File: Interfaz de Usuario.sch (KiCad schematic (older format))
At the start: 10 parts, among them J2 Conn_01x14, J3 Conn_02x04_Odd_Even, SW1 SW_Push_Dual

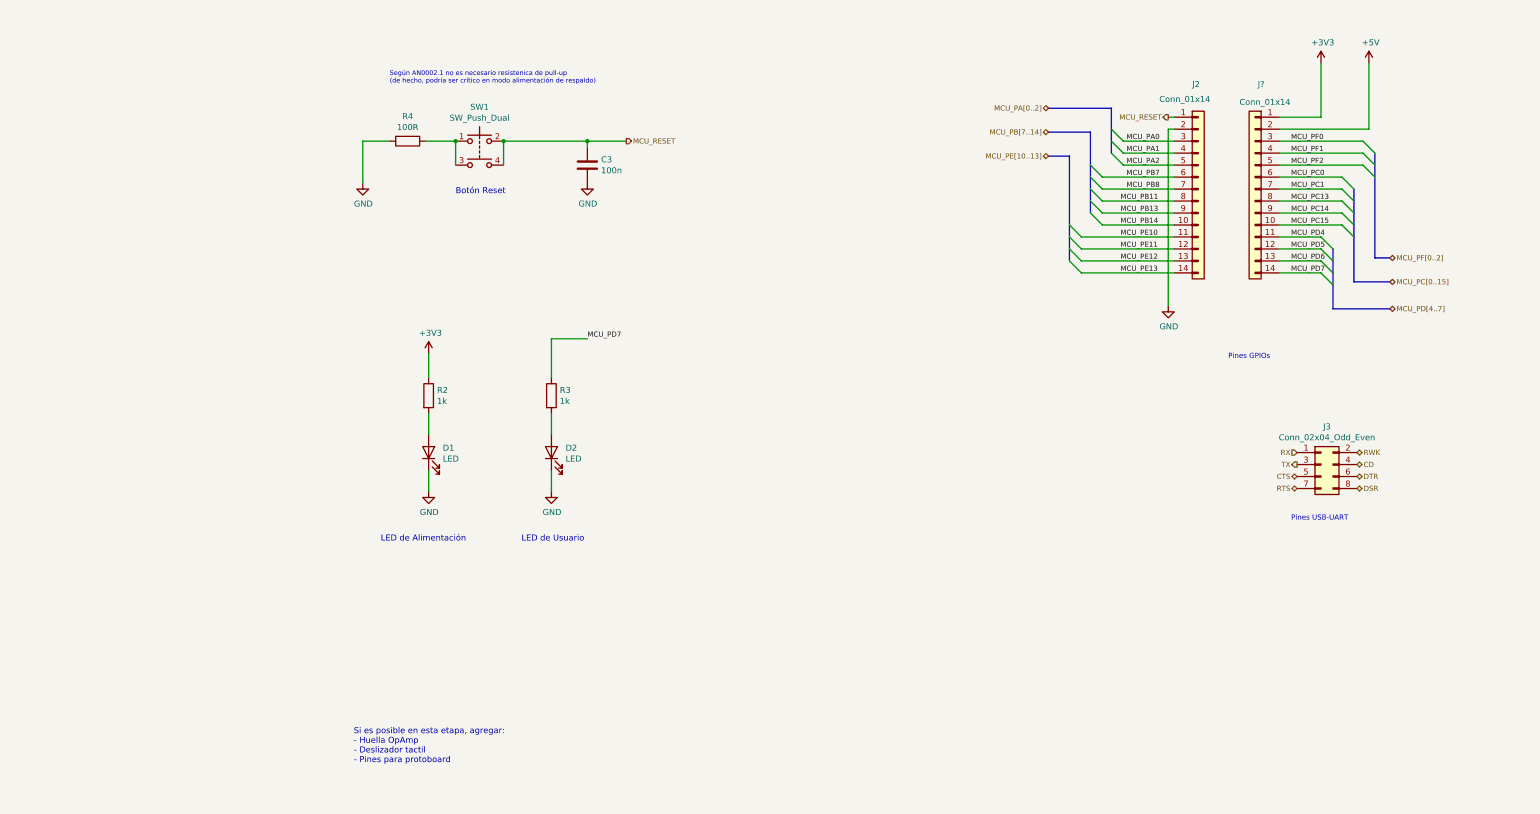
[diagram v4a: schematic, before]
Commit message: Issue #1: Incorporación de conector para debug
Se agrega el conector estandar para ARM de 10 pines para debug con SWD.
Como referencia use la nota de aplicación AN0002.1
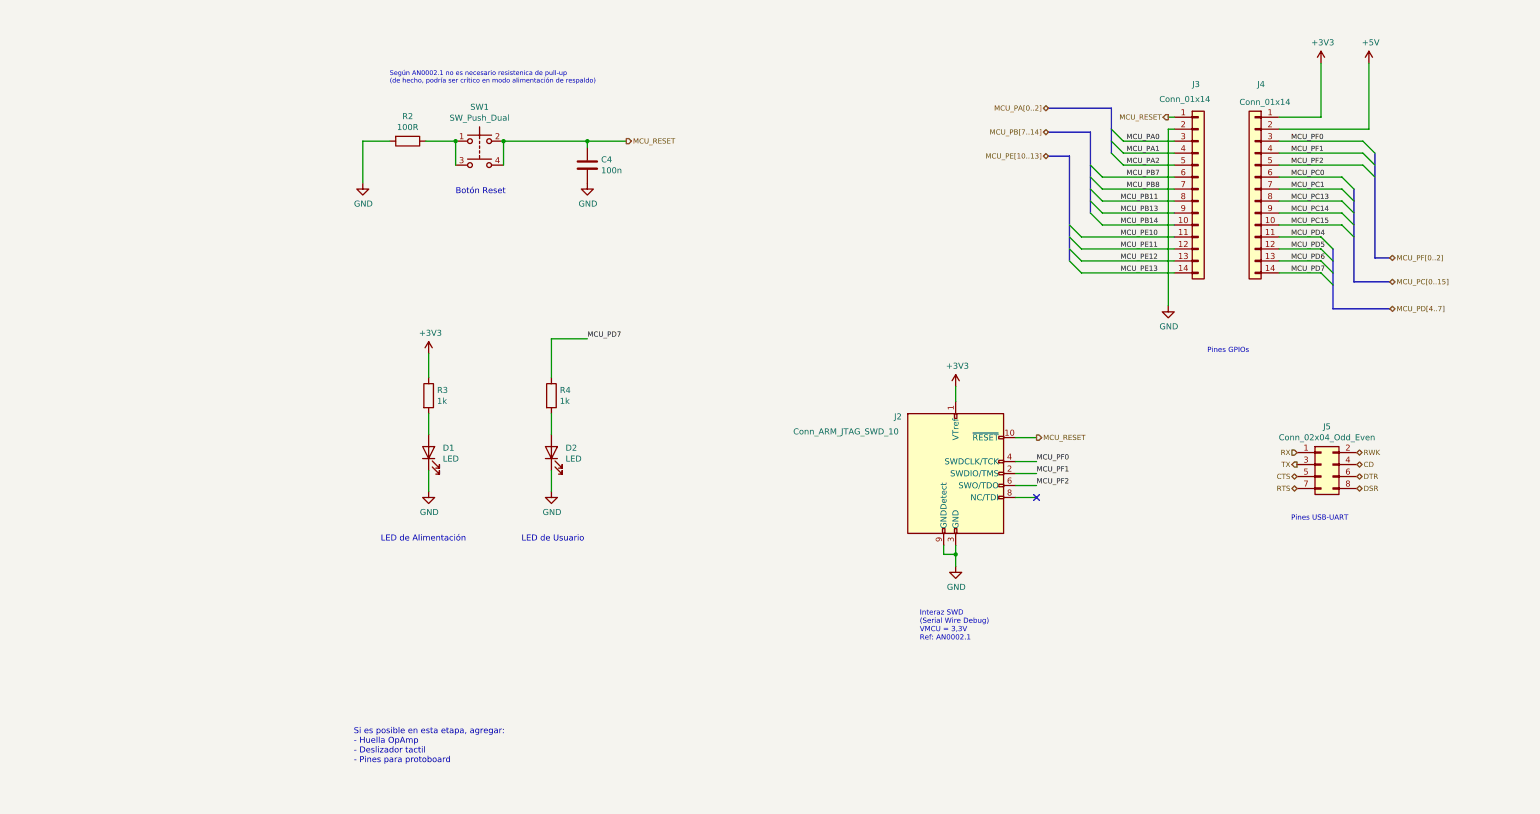
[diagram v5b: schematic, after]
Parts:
- added J2: Conn_ARM_JTAG_SWD_10, symbol Connector:Conn_ARM_JTAG_SWD_10
- gave numbers to parts that had none: 1
- renumbered C3 to C4, J2 to J3, J3 to J5, R4 to R2, R2 to R3, R3 to R4
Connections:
- net +3V3: now also J2.1 (VTref)
- net GND: now also J2.3 (GND), J2.5 (GND), J2.9 (GNDDetect)
- net MCU_PF0: now also J2.4 (SWDCLK/TCK)
- net MCU_PF1: now also J2.2 (SWDIO/TMS)
- net MCU_PF2: now also J2.6 (SWO/TDO)
- net MCU_RESET: now also J2.10 (~RESET~)
- no-connect marks 0 -> 1
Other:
- note added: "Interaz SWD\n(Serial Wire Debug)\nVMCU = 3,3V\nRef: AN0002.1"
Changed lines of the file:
@@
 $EndComp
 $Comp
-L Device:R R2
+L Device:R R3
 U 1 1 5F5B165F
 P 1600 4075
-F 0 "R2" H 1670 4121 50  0000 L CNN
+F 0 "R3" H 1670 4121 50  0000 L CNN
 F 1 "1k" H 1670 4030 50  0000 L CNN
 F 2 "" V 1530 4075 50  0001 C CNN
@@
 LED de Alimentación
 $Comp
-L power:+3V3 #PWR016
+L power:+3V3 #PWR015
 U 1 1 5F5B2737
 P 1600 3725
-F 0 "#PWR016" H 1600 3575 50  0001 C CNN
+F 0 "#PWR015" H 1600 3575 50  0001 C CNN
 F 1 "+3V3" H 1615 3898 50  0000 C CNN
 F 2 "" H 1600 3725 50  0001 C CNN
@@
 Pines USB-UART\n
 $Comp
-L power:+3V3 #PWR021
+L power:+3V3 #PWR022
 U 1 1 5F5DFF8C
 P 9050 1300
-F 0 "#PWR021" H 9050 1150 50  0001 C CNN
+F 0 "#PWR022" H 9050 1150 50  0001 C CNN
 F 1 "+3V3" H 9065 1473 50  0000 C CNN
 F 2 "" H 9050 1300 50  0001 C CNN
@@
 $EndComp
 $Comp
-L power:+5V #PWR022
+L power:+5V #PWR023
 U 1 1 5F5E0DA7
 P 9450 1300
-F 0 "#PWR022" H 9450 1150 50  0001 C CNN
+F 0 "#PWR023" H 9450 1150 50  0001 C CNN
 F 1 "+5V" H 9465 1473 50  0000 C CNN
 F 2 "" H 9450 1300 50  0001 C CNN
@@
 $EndComp
 $Comp
-L power:GND #PWR017
+L power:GND #PWR016
 U 1 1 5F5E177A
 P 1600 4875
-F 0 "#PWR017" H 1600 4625 50  0001 C CNN
+F 0 "#PWR016" H 1600 4625 50  0001 C CNN
 F 1 "GND" H 1605 4702 50  0000 C CNN
 F 2 "" H 1600 4875 50  0001 C CNN
@@
 $EndComp
 $Comp
-L power:GND #PWR020
+L power:GND #PWR021
 U 1 1 5F5E1C7B
 P 7775 3325
-F 0 "#PWR020" H 7775 3075 50  0001 C CNN
+F 0 "#PWR021" H 7775 3075 50  0001 C CNN
 F 1 "GND" H 7780 3152 50  0000 C CNN
 F 2 "" H 7775 3325 50  0001 C CNN
@@
 $EndComp
 $Comp
-L power:GND #PWR018
+L power:GND #PWR017
 U 1 1 5F61283E
 P 2625 4875
-F 0 "#PWR018" H 2625 4625 50  0001 C CNN
+F 0 "#PWR017" H 2625 4625 50  0001 C CNN
 F 1 "GND" H 2630 4702 50  0000 C CNN
 F 2 "" H 2625 4875 50  0001 C CNN
@@
 MCU_PD7
 $Comp
-L Device:R R3
+L Device:R R4
 U 1 1 5F61282A
 P 2625 4075
-F 0 "R3" H 2695 4121 50  0000 L CNN
+F 0 "R4" H 2695 4121 50  0000 L CNN
 F 1 "1k" H 2695 4030 50  0000 L CNN
 F 2 "" V 2555 4075 50  0001 C CNN
@@
 MCU_RESET
 $Comp
-L power:GND #PWR015
+L power:GND #PWR014
 U 1 1 5F61A6A2
 P 1050 2300
-F 0 "#PWR015" H 1050 2050 50  0001 C CNN
+F 0 "#PWR014" H 1050 2050 50  0001 C CNN
 F 1 "GND" H 1055 2127 50  0000 C CNN
 F 2 "" H 1050 2300 50  0001 C CNN
@@
 Wire Wire Line
 	1825 1950 1825 2150
-Text Notes 8275 3775 0    43   ~ 0
+Text Notes 8100 3725 0    43   ~ 0
 Pines GPIOs
 Text Label 7425 1950 0    43   ~ 0
@@
 MCU_RESET
 $Comp
-L Connector_Generic:Conn_02x04_Odd_Even J3
+L Connector_Generic:Conn_02x04_Odd_Even J5
 U 1 1 5F5CD54F
 P 9050 4650
-F 0 "J3" H 9100 4967 50  0000 C CNN
+F 0 "J5" H 9100 4967 50  0000 C CNN
 F 1 "Conn_02x04_Odd_Even" H 9100 4876 50  0000 C CNN
 F 2 "" H 9050 4650 50  0001 C CNN
@@
 Según AN0002.1 no es necesario resistenica de pull-up\n(de hecho, podría ser crítico en modo alimentación de respaldo)
 $Comp
-L Device:C C3
+L Device:C C4
 U 1 1 5F608348
 P 2925 2150
-F 0 "C3" H 3040 2196 50  0000 L CNN
+F 0 "C4" H 3040 2196 50  0000 L CNN
 F 1 "100n" H 3040 2105 50  0000 L CNN
 F 2 "" H 2963 2000 50  0001 C CNN
@@
 $EndComp
 $Comp
-L power:GND #PWR0101
+L power:GND #PWR018
 U 1 1 5F608A3C
 P 2925 2300
-F 0 "#PWR0101" H 2925 2050 50  0001 C CNN
+F 0 "#PWR018" H 2925 2050 50  0001 C CNN
 F 1 "GND" H 2930 2127 50  0000 C CNN
 F 2 "" H 2925 2300 50  0001 C CNN
@@
 $EndComp
 $Comp
-L Device:R R4
+L Device:R R2
 U 1 1 5F60A43B
 P 1425 1950
-F 0 "R4" V 1218 1950 50  0000 C CNN
+F 0 "R2" V 1218 1950 50  0000 C CNN
 F 1 "100R" V 1309 1950 50  0000 C CNN
 F 2 "" V 1355 1950 50  0001 C CNN
@@
 	1050 1950 1050 2300
 $Comp
-L Connector_Generic:Conn_01x14 J2
+L Connector_Generic:Conn_01x14 J3
 U 1 1 5F616B2C
 P 8025 2350
-F 0 "J2" H 7975 3225 50  0000 L CNN
+F 0 "J3" H 7975 3225 50  0000 L CNN
 F 1 "Conn_01x14" H 7700 3100 50  0000 L CNN
 F 2 "" H 8025 2350 50  0001 C CNN
@@
 $EndComp
 $Comp
-L Connector_Generic:Conn_01x14 J?
+L Connector_Generic:Conn_01x14 J4
 U 1 1 5F61A09A
 P 8500 2350
-F 0 "J?" H 8450 3225 50  0000 C CNN
+F 0 "J4" H 8450 3225 50  0000 C CNN
 F 1 "Conn_01x14" H 8418 3076 50  0000 C CNN
 F 2 "" H 8500 2350 50  0001 C CNN
@@
 	-1   0    0    -1
 $EndComp
+$Comp
+L Connector:Conn_ARM_JTAG_SWD_10 J2
+U 1 1 5F61E73C
+P 6000 4725
+F 0 "J2" H 5550 5200 50  0000 R CNN
+F 1 "Conn_ARM_JTAG_SWD_10" H 5525 5075 50  0000 R CNN
+F 2 "" H 6000 4725 50  0001 C CNN
+F 3 "http://infocenter.arm.com/help/topic/com.arm.doc.ddi0314h/DDI0314H_coresight_components_trm.pdf" V 5650 3475 50  0001 C CNN
+	1    6000 4725
+	1    0    0    -1
+$EndComp
+Wire Wire Line
+	6500 4425 6675 4425
+Wire Wire Line
+	6500 4625 6675 4625
+Wire Wire Line
+	6500 4725 6675 4725
+Wire Wire Line
+	6500 4825 6675 4825
+Wire Wire Line
+	6500 4925 6675 4925
+Wire Wire Line
+	6000 4125 6000 4000
+Text HLabel 6675 4425 2    43   Output ~ 0
+MCU_RESET
+Text Notes 5700 6125 0    43   ~ 0
+Interaz SWD\n(Serial Wire Debug)\nVMCU = 3,3V\nRef: AN0002.1
+$Comp
+L power:+3V3 #PWR019
+U 1 1 5F62A3CF
+P 6000 4000
+F 0 "#PWR019" H 6000 3850 50  0001 C CNN
+F 1 "+3V3" H 6015 4173 50  0000 C CNN
+F 2 "" H 6000 4000 50  0001 C CNN
+F 3 "" H 6000 4000 50  0001 C CNN
+	1    6000 4000
+	1    0    0    -1
+$EndComp
+Wire Wire Line
+	6000 5325 6000 5400
+Text Label 6675 4625 0    43   ~ 0
+MCU_PF0
+Text Label 6675 4725 0    43   ~ 0
+MCU_PF1
+Text Label 6675 4825 0    43   ~ 0
+MCU_PF2
+$Comp
+L power:GND #PWR020
+U 1 1 5F6334C6
+P 6000 5500
+F 0 "#PWR020" H 6000 5250 50  0001 C CNN
+F 1 "GND" H 6005 5327 50  0000 C CNN
+F 2 "" H 6000 5500 50  0001 C CNN
+F 3 "" H 6000 5500 50  0001 C CNN
+	1    6000 5500
+	1    0    0    -1
+$EndComp
+Wire Wire Line
+	5900 5325 5900 5400
+Wire Wire Line
+	5900 5400 6000 5400
+Connection ~ 6000 5400
+Wire Wire Line
+	6000 5400 6000 5500
+NoConn ~ 6675 4925
 Wire Bus Line
 	7300 1675 7300 2050

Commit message: Issue #1: Se agregan LEDs para líneas TX/RX de UART
Se agregan los LEDs para indicar comunicación vía UART. Se utilizó un
OpAmp para evitar un consumo excesivo de corriente en las líneas de
comunicación.

Referencia: https://bit.ly/2E7PuVE
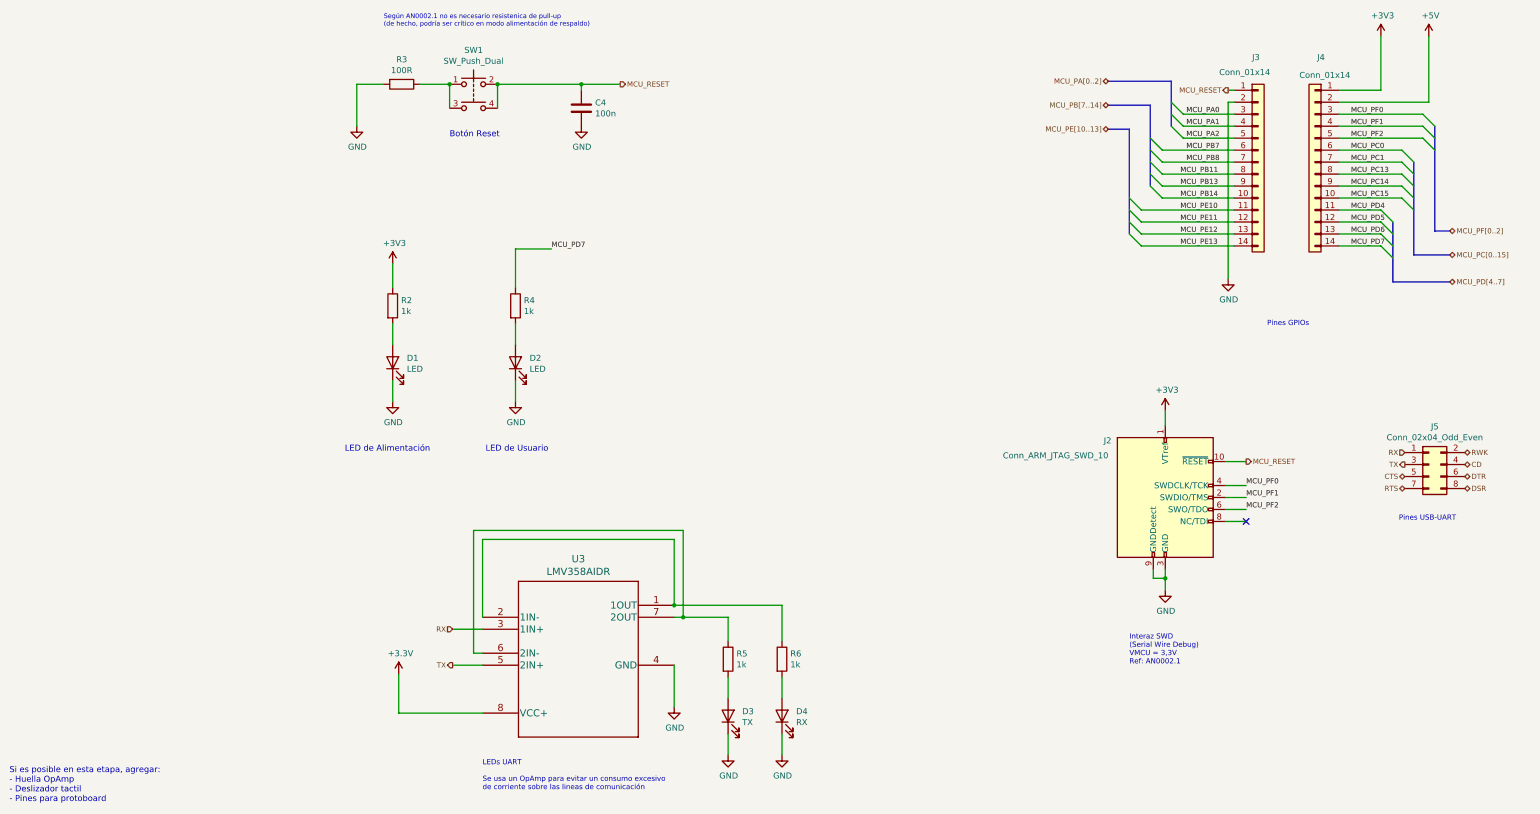
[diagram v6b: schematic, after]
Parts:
- added D3: TX, symbol Device:LED
- added D4: RX, symbol Device:LED
- added R5, R6: 1k, symbol Device:R
- added U3: LMV358AIDR, D8_TEX, symbol LMV358AIDR:LMV358AIDR
- renumbered R3 to R2, R2 to R3
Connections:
- net +3V3: now also U3.8 (VCC+)
- net GND: now also D3.1 (K), D4.1 (K), U3.4 (GND)
- net RX: now also U3.3 (1IN+)
- net TX: now also U3.5 (2IN+)
- new net: R6.1, U3.1 (1OUT), U3.2 (1IN-)
- new net: R5.1, U3.6 (2IN-), U3.7 (2OUT)
- new net: D3.2 (A), R5.2
- new net: D4.2 (A), R6.2
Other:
- note added: "LEDs UART\n\nSe usa un OpAmp para evitar un consumo excesivo\nde corriente sobre las lineas de comunicación"
- moved on the sheet: C4, D1, D2, J2, J3, J4, J5, R2, R3, R4, SW1

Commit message: Issue #2: Primer acercamiento al diseño de la PCB
Se modificaron los conectores externos de los pines GPIOs (para no
exponer los que se conectan a los cristales) y se realizó la
distribución inicial de componentes en la placa (sin conectarlos)
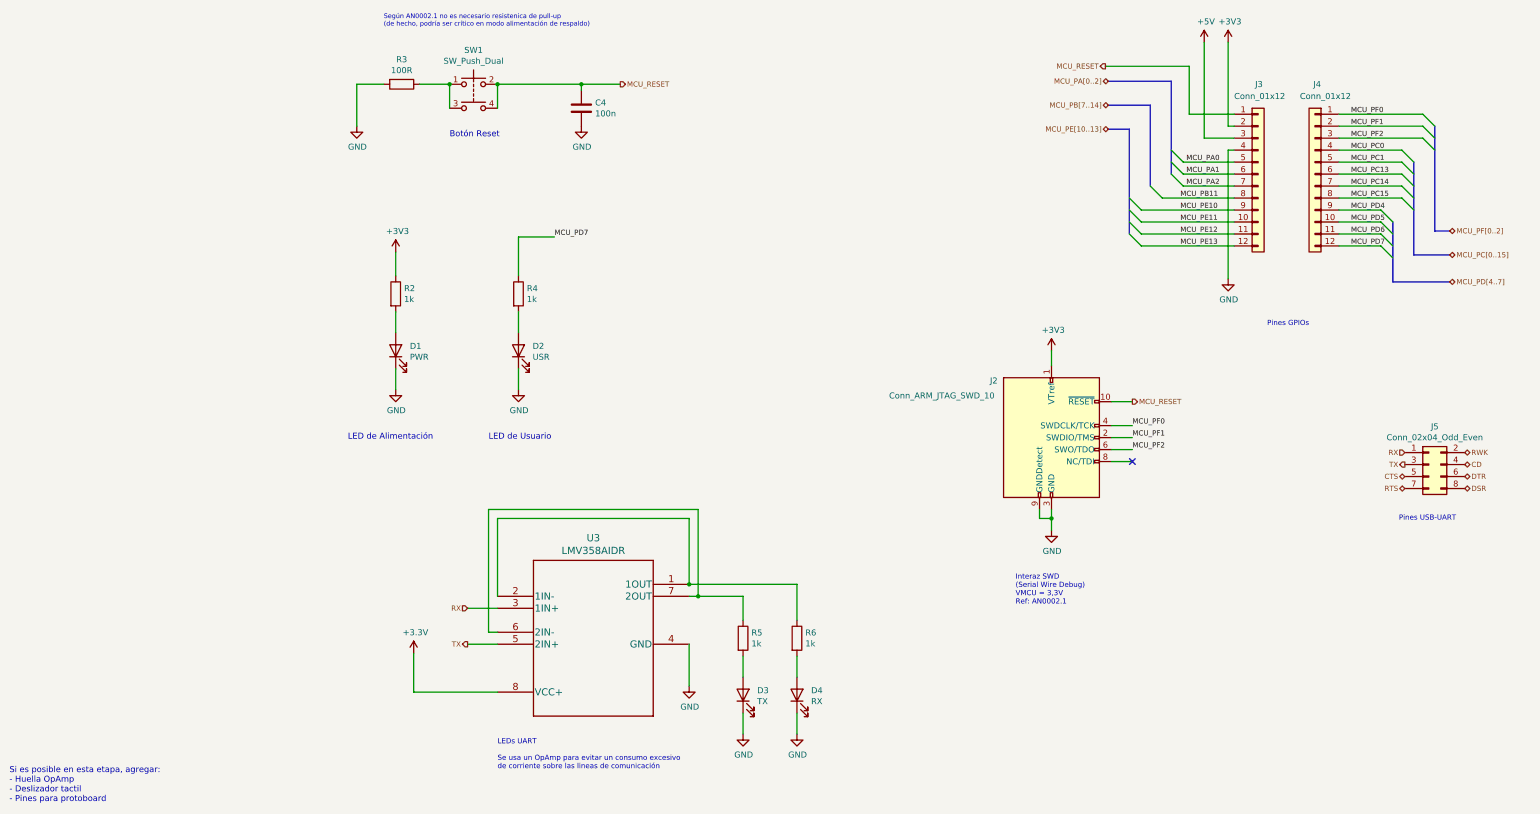
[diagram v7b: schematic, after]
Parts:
- removed J3, J4: Conn_01x14, symbol Connector_Generic:Conn_01x14
- added J3, J4: Conn_01x12, Connector_PinHeader_2.54mm:PinHeader_1x12_P2.54mm_Vertical, symbol Connector_Generic:Conn_01x12
- C4: footprint (none) -> Capacitor_SMD:C_0603_1608Metric_Pad1.05x0.95mm_HandSolder
- D1: value LED -> PWR; footprint (none) -> LED_SMD:LED_0603_1608Metric_Pad1.05x0.95mm_HandSolder
- D2: value LED -> USR; footprint (none) -> LED_SMD:LED_0603_1608Metric_Pad1.05x0.95mm_HandSolder
- D3, D4: footprint (none) -> LED_SMD:LED_0603_1608Metric_Pad1.05x0.95mm_HandSolder
- J2: footprint (none) -> Connector_PinHeader_1.00mm:PinHeader_2x05_P1.00mm_Vertical_SMD
- J5: footprint (none) -> Connector_PinHeader_2.54mm:PinHeader_2x04_P2.54mm_Vertical_SMD
- R2, R3, R4, R5, R6: footprint (none) -> Resistor_SMD:R_0603_1608Metric_Pad1.05x0.95mm_HandSolder
- SW1: footprint (none) -> Button_Switch_THT:SW_TH_Tactile_Omron_B3F-10xx
- U3: footprint D8_TEX -> Mis Huellas:LMV358AIDR
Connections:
- net +3V3: now also J3.2 (Pin_2)
- net +5V: now also J3.3 (Pin_3)
- net GND: now also J3.4 (Pin_4)
- net MCU_PA0: now also J3.5 (Pin_5)
- net MCU_PA1: now also J3.6 (Pin_6)
- net MCU_PA2: now also J3.7 (Pin_7)
- net MCU_PB11: now also J3.8 (Pin_8)
- net MCU_PC0: now also J4.4 (Pin_4)
- net MCU_PC1: now also J4.5 (Pin_5)
- net MCU_PC13: now also J4.6 (Pin_6)
- net MCU_PC14: now also J4.7 (Pin_7)
- net MCU_PC15: now also J4.8 (Pin_8)
- net MCU_PD4: now also J4.9 (Pin_9)
- net MCU_PD5: now also J4.10 (Pin_10)
- net MCU_PD6: now also J4.11 (Pin_11)
- net MCU_PD7: now also J4.12 (Pin_12)
- net MCU_PE10: now also J3.9 (Pin_9)
- net MCU_PE11: now also J3.10 (Pin_10)
- net MCU_PE12: now also J3.11 (Pin_11)
- net MCU_PE13: now also J3.12 (Pin_12)
- net MCU_PF0: now also J4.1 (Pin_1)
- net MCU_PF1: now also J4.2 (Pin_2)
- net MCU_PF2: now also J4.3 (Pin_3)
- net MCU_RESET: now also J3.1 (Pin_1)
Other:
- moved on the sheet: D1, D2, D3, D4, J2, R2, R4, R5, R6, U3

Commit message: Issue #2: PCB lista para primera prueba de concepto
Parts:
- removed J3, J4: Conn_01x12, Connector_PinHeader_2.54mm:PinHeader_1x12_P2.54mm_Vertical, symbol Connector_Generic:Conn_01x12
- removed J5: Conn_02x04_Odd_Even, Connector_PinHeader_2.54mm:PinHeader_2x04_P2.54mm_Vertical_SMD, symbol Connector_Generic:Conn_02x04_Odd_Even
- added J3, J4: Conn_01x11, Connector_PinHeader_2.54mm:PinHeader_1x11_P2.54mm_Vertical, symbol Connector_Generic:Conn_01x11
- C4: footprint Capacitor_SMD:C_0603_1608Metric_Pad1.05x0.95mm_HandSolder -> Capacitor_SMD:C_1206_3216Metric_Pad1.42x1.75mm_HandSolder
- D1, D2, D3, D4: footprint LED_SMD:LED_0603_1608Metric_Pad1.05x0.95mm_HandSolder -> LED_SMD:LED_1206_3216Metric
- R2: footprint Resistor_SMD:R_0603_1608Metric_Pad1.05x0.95mm_HandSolder -> Resistor_SMD:R_1206_3216Metric_Pad1.42x1.75mm_HandSolder
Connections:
- net +3V3: now also J3.2 (Pin_2)
- net +5V: now also J3.1 (Pin_1)
- net GND: now also J3.3 (Pin_3)
- net MCU_PA0: now also J3.4 (Pin_4)
- net MCU_PA1: now also J3.5 (Pin_5)
- net MCU_PA2: now also J3.6 (Pin_6)
- net MCU_PB11: now also J3.10 (Pin_10)
- net MCU_PC0: now also J3.7 (Pin_7)
- net MCU_PC1: now also J3.8 (Pin_8)
- net MCU_PC13: now also J4.8 (Pin_8)
- net MCU_PC14: now also J4.7 (Pin_7)
- net MCU_PC15: now also J4.6 (Pin_6)
- net MCU_PD4: now also J3.11 (Pin_11)
- net MCU_PD5: now also J4.11 (Pin_11)
- net MCU_PD6: now also J4.10 (Pin_10)
- net MCU_PD7: now also J4.9 (Pin_9)
- net MCU_PE10: now also J4.4 (Pin_4)
- net MCU_PE11: now also J4.3 (Pin_3)
- net MCU_PE12: now also J4.2 (Pin_2)
- net MCU_PE13: now also J4.1 (Pin_1)
- net MCU_PF2: now also J4.5 (Pin_5)
- net MCU_RESET: now also J3.9 (Pin_9)
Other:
- note removed: "Pines USB-UART\n"
